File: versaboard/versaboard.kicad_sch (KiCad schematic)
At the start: 23 parts, among them J3 UART, J39 Conn_02x20_Odd_Even, J4 DBG, J40 Conn_02x20_Odd_Even, SW1 RST, U1 ATSAML21G18B-AUT, Y1 32.768kHz

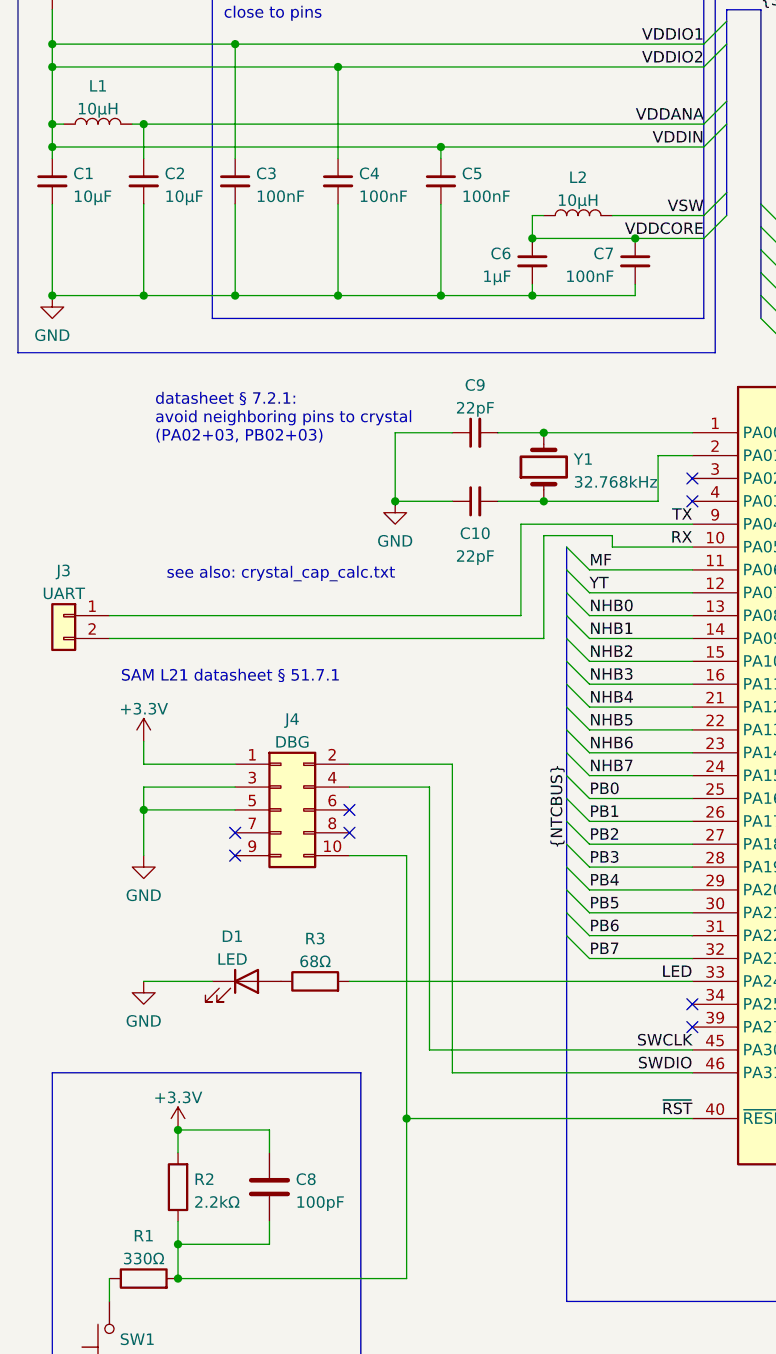
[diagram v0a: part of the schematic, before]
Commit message: versaboard: geographic reannotate
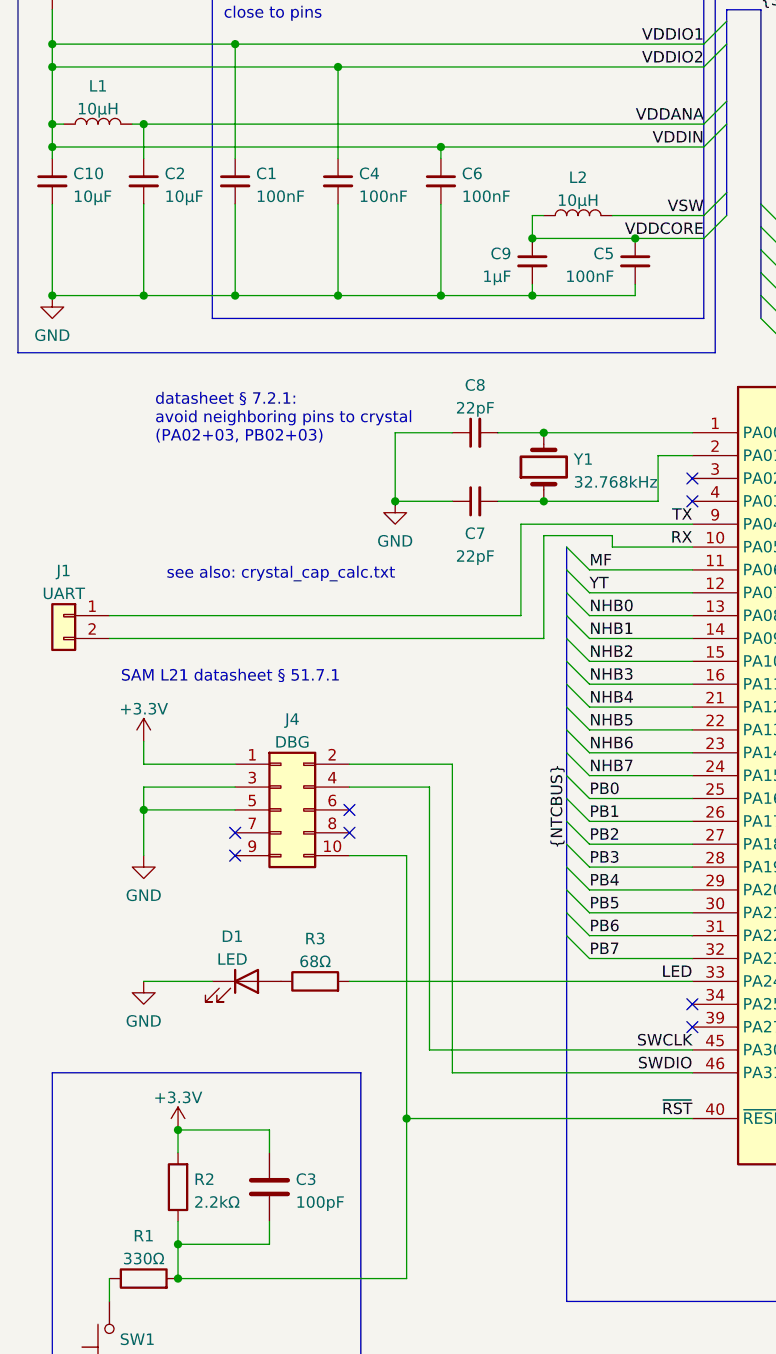
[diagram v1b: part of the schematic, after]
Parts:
- renumbered C3 to C1, C1 to C10, C8 to C3, C7 to C5, C5 to C6, C10 to C7, C9 to C8, C6 to C9, J3 to J1
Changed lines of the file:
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@@
   (symbol (lib_id "Device:C_Small") (at 66.04 67.31 90) (unit 1)
     (in_bom yes) (on_board yes)
-    (property "Reference" "C9" (id 0) (at 66.0463 62.0481 90))
+    (property "Reference" "C8" (id 0) (at 66.0463 62.0481 90))
     (property "Value" "22pF" (id 1) (at 66.0463 64.585 90))
     (property "Footprint" "Capacitor_SMD:C_0402_1005Metric" (id 2) (at 66.04 67.31 0)
@@
   (symbol (lib_id "Device:C_Small") (at 66.04 74.93 90) (unit 1)
     (in_bom yes) (on_board yes) (fields_autoplaced)
-    (property "Reference" "C10" (id 0) (at 66.0463 78.5225 90))
+    (property "Reference" "C7" (id 0) (at 66.0463 78.5225 90))
     (property "Value" "22pF" (id 1) (at 66.0463 81.0594 90))
     (property "Footprint" "Capacitor_SMD:C_0402_1005Metric" (id 2) (at 66.04 74.93 0)
@@
   (symbol (lib_id "Device:C") (at 43.18 151.13 0) (unit 1)
     (in_bom yes) (on_board yes) (fields_autoplaced)
-    (property "Reference" "C8" (id 0) (at 46.101 150.2953 0)
+    (property "Reference" "C3" (id 0) (at 46.101 150.2953 0)
       (effects (font (size 1.27 1.27)) (justify left))
     )
@@
   (symbol (lib_id "Device:C_Small") (at 19.05 39.37 0) (unit 1)
     (in_bom yes) (on_board yes) (fields_autoplaced)
-    (property "Reference" "C1" (id 0) (at 21.3741 38.5416 0)
+    (property "Reference" "C10" (id 0) (at 21.3741 38.5416 0)
       (effects (font (size 1.27 1.27)) (justify left))
     )
@@
   (symbol (lib_id "Connector_Generic:Conn_01x02") (at 20.32 87.63 0) (mirror y) (unit 1)
     (in_bom yes) (on_board yes) (fields_autoplaced)
-    (property "Reference" "J3" (id 0) (at 20.32 82.6602 0))
+    (property "Reference" "J1" (id 0) (at 20.32 82.6602 0))
     (property "Value" "UART" (id 1) (at 20.32 85.1971 0))
     (property "Footprint" "Connector_PinHeader_2.54mm_Horizontal_SMD:Samtec_TSM-102-01-L-SH" (id 2) (at 20.32 87.63 0)
@@
   (symbol (lib_id "Device:C_Small") (at 39.37 39.37 0) (unit 1)
     (in_bom yes) (on_board yes) (fields_autoplaced)
-    (property "Reference" "C3" (id 0) (at 41.6941 38.5416 0)
+    (property "Reference" "C1" (id 0) (at 41.6941 38.5416 0)
       (effects (font (size 1.27 1.27)) (justify left))
     )
@@
   (symbol (lib_id "Device:C_Small") (at 62.23 39.37 0) (unit 1)
     (in_bom yes) (on_board yes) (fields_autoplaced)
-    (property "Reference" "C5" (id 0) (at 64.5541 38.5416 0)
+    (property "Reference" "C6" (id 0) (at 64.5541 38.5416 0)
       (effects (font (size 1.27 1.27)) (justify left))
     )
@@
   (symbol (lib_id "Device:C_Small") (at 72.39 48.26 0) (unit 1)
     (in_bom yes) (on_board yes) (fields_autoplaced)
-    (property "Reference" "C6" (id 0) (at 70.0659 47.4316 0)
+    (property "Reference" "C9" (id 0) (at 70.0659 47.4316 0)
       (effects (font (size 1.27 1.27)) (justify right))
     )
@@
   (symbol (lib_id "Device:C_Small") (at 83.82 48.26 0) (unit 1)
     (in_bom yes) (on_board yes) (fields_autoplaced)
-    (property "Reference" "C7" (id 0) (at 81.4959 47.4316 0)
+    (property "Reference" "C5" (id 0) (at 81.4959 47.4316 0)
       (effects (font (size 1.27 1.27)) (justify right))
     )
@@
       (reference "#PWR011") (unit 1) (value "GND") (footprint "")
     )
-    (path "/ba22a4b5-95b0-4de5-bced-f545f86d8229"
-      (reference "C1") (unit 1) (value "10µF") (footprint "Capacitor_SMD:C_0603_1608Metric")
+    (path "/cc683378-fbf8-420a-afab-c6a9069a0f20"
+      (reference "C1") (unit 1) (value "100nF") (footprint "Capacitor_SMD:C_0402_1005Metric")
     )
     (path "/a7e945e6-c1a1-4716-b3f8-ea9ce2bf633f"
       (reference "C2") (unit 1) (value "10µF") (footprint "Capacitor_SMD:C_0603_1608Metric")
     )
-    (path "/cc683378-fbf8-420a-afab-c6a9069a0f20"
-      (reference "C3") (unit 1) (value "100nF") (footprint "Capacitor_SMD:C_0402_1005Metric")
+    (path "/7b0f8545-ffda-4d14-beb8-344e4fcf1147"
+      (reference "C3") (unit 1) (value "100pF") (footprint "Capacitor_SMD:C_0402_1005Metric")
     )
     (path "/2e487413-87bd-4d87-b2ac-edcaab79cdeb"
       (reference "C4") (unit 1) (value "100nF") (footprint "Capacitor_SMD:C_0402_1005Metric")
     )
+    (path "/f4c30170-e598-4fb7-8fad-ba1a06e429da"
+      (reference "C5") (unit 1) (value "100nF") (footprint "Capacitor_SMD:C_0402_1005Metric")
+    )
     (path "/d06f6168-2c46-4287-8dcf-019302173d6b"
-      (reference "C5") (unit 1) (value "100nF") (footprint "Capacitor_SMD:C_0402_1005Metric")
+      (reference "C6") (unit 1) (value "100nF") (footprint "Capacitor_SMD:C_0402_1005Metric")
+    )
+    (path "/6c31e4fd-257d-4d7c-933c-2839f0d41380"
+      (reference "C7") (unit 1) (value "22pF") (footprint "Capacitor_SMD:C_0402_1005Metric")
+    )
+    (path "/51baac91-df86-4110-b919-9139d7ff8cdd"
+      (reference "C8") (unit 1) (value "22pF") (footprint "Capacitor_SMD:C_0402_1005Metric")
     )
     (path "/e0f83ba9-d078-481f-957a-b544aee953b8"
-      (reference "C6") (unit 1) (value "1µF") (footprint "Capacitor_SMD:C_0402_1005Metric")
-    )
-    (path "/f4c30170-e598-4fb7-8fad-ba1a06e429da"
-      (reference "C7") (unit 1) (value "100nF") (footprint "Capacitor_SMD:C_0402_1005Metric")
-    )
-    (path "/7b0f8545-ffda-4d14-beb8-344e4fcf1147"
-      (reference "C8") (unit 1) (value "100pF") (footprint "Capacitor_SMD:C_0402_1005Metric")
-    )
-    (path "/51baac91-df86-4110-b919-9139d7ff8cdd"
-      (reference "C9") (unit 1) (value "22pF") (footprint "Capacitor_SMD:C_0402_1005Metric")
-    )
-    (path "/6c31e4fd-257d-4d7c-933c-2839f0d41380"
-      (reference "C10") (unit 1) (value "22pF") (footprint "Capacitor_SMD:C_0402_1005Metric")
+      (reference "C9") (unit 1) (value "1µF") (footprint "Capacitor_SMD:C_0402_1005Metric")
+    )
+    (path "/ba22a4b5-95b0-4de5-bced-f545f86d8229"
+      (reference "C10") (unit 1) (value "10µF") (footprint "Capacitor_SMD:C_0603_1608Metric")
     )
     (path "/6ec904da-9876-48ea-a365-c0d5d54818df"
@@
     )
     (path "/c6139276-1e28-4f65-895c-612087a5a2e2"
-      (reference "J3") (unit 1) (value "UART") (footprint "Connector_PinHeader_2.54mm_Horizontal_SMD:Samtec_TSM-102-01-L-SH")
+      (reference "J1") (unit 1) (value "UART") (footprint "Connector_PinHeader_2.54mm_Horizontal_SMD:Samtec_TSM-102-01-L-SH")
     )
     (path "/70edb921-d540-409b-a2bc-8cb5d54d65a6"

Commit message: versaboard: add LCSC numbers
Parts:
- C1, C4, C5, C6: LCSC (none) -> C307331
- C10, C2: LCSC (none) -> C19702
- C3: LCSC (none) -> C1546
- C7, C8: LCSC (none) -> C1555
- C9: LCSC (none) -> C52923
- D1: LCSC (none) -> C72038
- J39, J40: LCSC (none) -> C2685111
- J4: LCSC (none) -> C5250218
- L1, L2: LCSC (none) -> C1035
- R1: LCSC (none) -> C25104
- R2: LCSC (none) -> C25879
- R3: LCSC (none) -> C27592
- SW1: LCSC (none) -> C393942
- U1: LCSC (none) -> C619131
- Y1: LCSC (none) -> C32346
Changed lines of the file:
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@@
+      (effects (font (size 1.27 1.27)) hide)
+    )
+    (property "LCSC" "C619131" (id 5) (at 120.1294 150.6204 0)
       (effects (font (size 1.27 1.27)) hide)
     )
@@
       (effects (font (size 1.27 1.27)) hide)
     )
+    (property "LCSC" "C1035" (id 5) (at 77.47 38.9722 0)
+      (effects (font (size 1.27 1.27)) hide)
+    )
     (pin "1")
     (pin "2")
@@
       (effects (font (size 1.27 1.27)) hide)
     )
+    (property "LCSC" "C307331" (id 5) (at 53.1241 38.5416 0)
+      (effects (font (size 1.27 1.27)) hide)
+    )
     (pin "1")
     (pin "2")
@@
     )
     (property "JLCPCB" "C25879" (id 4) (at 33.02 151.13 0)
+      (effects (font (size 1.27 1.27)) hide)
+    )
+    (property "LCSC" "C25879" (id 5) (at 34.798 150.2953 0)
       (effects (font (size 1.27 1.27)) hide)
     )
@@
     )
     (property "JLCPCB" "C25104" (id 4) (at 29.21 161.29 0)
+      (effects (font (size 1.27 1.27)) hide)
+    )
+    (property "LCSC" "C25104" (id 5) (at 29.21 156.5742 0)
       (effects (font (size 1.27 1.27)) hide)
     )
@@
       (effects (font (size 1.27 1.27)) hide)
     )
+    (property "LCSC" "C1555" (id 5) (at 66.0463 62.0481 0)
+      (effects (font (size 1.27 1.27)) hide)
+    )
     (pin "1")
     (pin "2")
@@
     )
     (property "JLCPCB" "C2685111" (id 4) (at 223.52 120.65 0)
+      (effects (font (size 1.27 1.27)) hide)
+    )
+    (property "LCSC" "C2685111" (id 5) (at 198.628 118.5453 0)
       (effects (font (size 1.27 1.27)) hide)
     )
@@
       (effects (font (size 1.27 1.27)) hide)
     )
+    (property "LCSC" "C32346" (id 5) (at 76.9874 70.2853 0)
+      (effects (font (size 1.27 1.27)) hide)
+    )
     (pin "1")
     (pin "2")
@@
       (effects (font (size 1.27 1.27)) hide)
     )
+    (property "LCSC" "C1555" (id 5) (at 66.0463 78.5225 0)
+      (effects (font (size 1.27 1.27)) hide)
+    )
     (pin "1")
     (pin "2")
@@
       (effects (font (size 1.27 1.27)) hide)
     )
+    (property "LCSC" "C72038" (id 5) (at 39.0525 123.3002 0)
+      (effects (font (size 1.27 1.27)) hide)
+    )
     (pin "1")
     (pin "2")
@@
     )
     (property "JLCPCB" "C5250218" (id 5) (at 44.45 109.22 0)
+      (effects (font (size 1.27 1.27)) hide)
+    )
+    (property "LCSC" "C5250218" (id 6) (at 45.72 99.1702 0)
       (effects (font (size 1.27 1.27)) hide)
     )
@@
       (effects (font (size 1.27 1.27)) hide)
     )
+    (property "LCSC" "C1546" (id 5) (at 46.101 150.2953 0)
+      (effects (font (size 1.27 1.27)) hide)
+    )
     (pin "1")
     (pin "2")
@@
       (effects (font (size 1.27 1.27)) hide)
     )
+    (property "LCSC" "C393942" (id 5) (at 26.543 168.0753 0)
+      (effects (font (size 1.27 1.27)) hide)
+    )
     (pin "1")
     (pin "2")
@@
     )
     (property "JLCPCB" "C2685111" (id 4) (at 224.79 88.9 0)
+      (effects (font (size 1.27 1.27)) hide)
+    )
+    (property "LCSC" "C2685111" (id 5) (at 199.898 86.7953 0)
       (effects (font (size 1.27 1.27)) hide)
     )
@@
       (effects (font (size 1.27 1.27)) hide)
     )
+    (property "LCSC" "C19702" (id 5) (at 31.5341 38.5416 0)
+      (effects (font (size 1.27 1.27)) hide)
+    )
     (pin "1")
     (pin "2")
@@
     )
     (property "JLCPCB" "C19702" (id 4) (at 19.05 39.37 0)
+      (effects (font (size 1.27 1.27)) hide)
+    )
+    (property "LCSC" "C19702" (id 5) (at 21.3741 38.5416 0)
       (effects (font (size 1.27 1.27)) hide)
     )
@@
       (effects (font (size 1.27 1.27)) hide)
     )
+    (property "LCSC" "C307331" (id 5) (at 41.6941 38.5416 0)
+      (effects (font (size 1.27 1.27)) hide)
+    )
     (pin "1")
     (pin "2")
@@
     )
     (property "JLCPCB" "C307331" (id 4) (at 62.23 39.37 0)
+      (effects (font (size 1.27 1.27)) hide)
+    )
+    (property "LCSC" "C307331" (id 5) (at 64.5541 38.5416 0)
       (effects (font (size 1.27 1.27)) hide)
     )
@@
       (effects (font (size 1.27 1.27)) hide)
     )
+    (property "LCSC" "C27592" (id 5) (at 48.26 123.5542 0)
+      (effects (font (size 1.27 1.27)) hide)
+    )
     (pin "1")
     (pin "2")
@@
     )
     (property "JLCPCB" "C52923" (id 4) (at 72.39 48.26 0)
+      (effects (font (size 1.27 1.27)) hide)
+    )
+    (property "LCSC" "C52923" (id 5) (at 70.0659 47.4316 0)
       (effects (font (size 1.27 1.27)) hide)
     )
@@
       (effects (font (size 1.27 1.27)) hide)
     )
+    (property "LCSC" "C1035" (id 5) (at 24.13 28.8122 0)
+      (effects (font (size 1.27 1.27)) hide)
+    )
     (pin "1")
     (pin "2")
@@
       (effects (font (size 1.27 1.27)) hide)
     )
+    (property "LCSC" "C307331" (id 5) (at 81.4959 47.4316 0)
+      (effects (font (size 1.27 1.27)) hide)
+    )

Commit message: versaboard: add JLCPCB mounting holes
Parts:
- J1: Device (none) -> Samtec TSM-102-01-L-SH-P; JLCPCB C5142235 -> C9900035116; LCSC (none) -> C9900035116
- U1: JLCPCB C619131 -> C2052742; LCSC C619131 -> C2052742
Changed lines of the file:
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@@
       (effects (font (size 1.27 1.27)) hide)
     )
-    (property "JLCPCB" "C619131" (id 4) (at 115.57 105.41 0)
-      (effects (font (size 1.27 1.27)) hide)
-    )
-    (property "LCSC" "C619131" (id 5) (at 120.1294 150.6204 0)
+    (property "JLCPCB" "C2052742" (id 4) (at 115.57 105.41 0)
+      (effects (font (size 1.27 1.27)) hide)
+    )
+    (property "LCSC" "C2052742" (id 5) (at 120.1294 150.6204 0)
       (effects (font (size 1.27 1.27)) hide)
     )
@@
       (effects (font (size 1.27 1.27)) hide)
     )
-    (property "JLCPCB" "C5142235" (id 4) (at 20.32 87.63 0)
-      (effects (font (size 1.27 1.27)) hide)
-    )
+    (property "JLCPCB" "C9900035116" (id 4) (at 20.32 87.63 0)
+      (effects (font (size 1.27 1.27)) hide)
+    )
+    (property "Device" "Samtec TSM-102-01-L-SH-P" (id 5) (at 20.32 87.63 0)
+      (effects (font (size 1.27 1.27)) hide)
+    )
+    (property "LCSC" "C9900035116" (id 6) (at 20.32 87.63 0)
+      (effects (font (size 1.27 1.27)) hide)
+    )
